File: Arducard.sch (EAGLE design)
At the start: 18 parts, among them U1 ATMEGA328P, U2 MPR121V2, U3 TPS61097-33DBVR, Y1 8MHZ

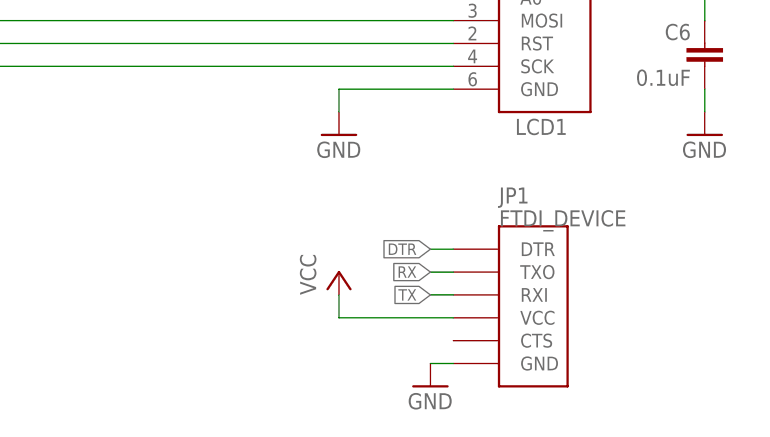
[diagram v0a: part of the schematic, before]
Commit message: Arducard Schematic (Eagle)
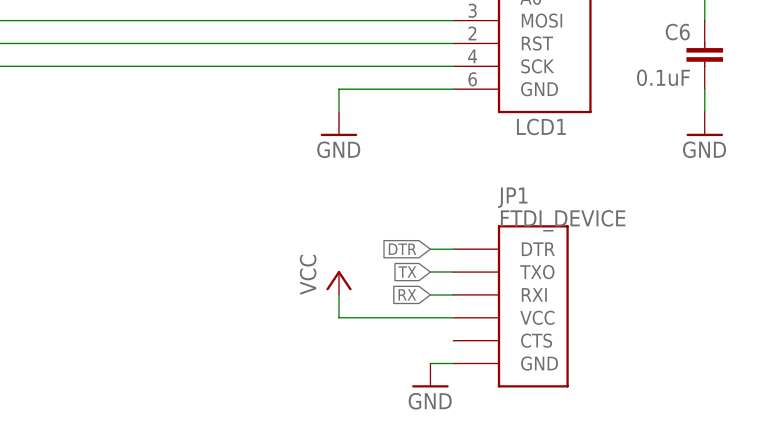
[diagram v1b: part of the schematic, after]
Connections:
- net RX: now also JP1.RXI; no longer JP1.TXO
- net TX: now also JP1.TXO; no longer JP1.RXI
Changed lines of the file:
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@@
 <net name="RX" class="0">
+<segment>
+<pinref part="U1" gate="G$1" pin="PD0(RXD)"/>
+<wire x1="124.46" y1="60.96" x2="127" y2="60.96" width="0.1524" layer="91"/>
+<label x="127" y="60.96" size="1.27" layer="91" xref="yes"/>
+</segment>
+<segment>
+<pinref part="JP1" gate="G$1" pin="RXI"/>
+<wire x1="180.34" y1="2.54" x2="177.8" y2="2.54" width="0.1524" layer="91"/>
+<label x="177.8" y="2.54" size="1.27" layer="91" rot="R180" xref="yes"/>
+</segment>
+</net>
+<net name="TX" class="0">
+<segment>
+<pinref part="U1" gate="G$1" pin="PD1(TXD)"/>
+<wire x1="124.46" y1="58.42" x2="127" y2="58.42" width="0.1524" layer="91"/>
+<label x="127" y="58.42" size="1.27" layer="91" xref="yes"/>
+</segment>
 <segment>
 <pinref part="JP1" gate="G$1" pin="TXO"/>
@@
 <label x="177.8" y="5.08" size="1.27" layer="91" rot="R180" xref="yes"/>
 </segment>
-<segment>
-<pinref part="U1" gate="G$1" pin="PD0(RXD)"/>
-<wire x1="124.46" y1="60.96" x2="127" y2="60.96" width="0.1524" layer="91"/>
-<label x="127" y="60.96" size="1.27" layer="91" xref="yes"/>
-</segment>
 </net>
-<net name="TX" class="0">
-<segment>
-<pinref part="JP1" gate="G$1" pin="RXI"/>
-<wire x1="180.34" y1="2.54" x2="177.8" y2="2.54" width="0.1524" layer="91"/>
-<label x="177.8" y="2.54" size="1.27" layer="91" rot="R180" xref="yes"/>
-</segment>
-<segment>
-<pinref part="U1" gate="G$1" pin="PD1(TXD)"/>
-<wire x1="124.46" y1="58.42" x2="127" y2="58.42" width="0.1524" layer="91"/>
-<label x="127" y="58.42" size="1.27" layer="91" xref="yes"/>
-</segment>
-</net>
